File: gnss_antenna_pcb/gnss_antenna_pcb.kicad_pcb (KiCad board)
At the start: 2 copper layers, 100 x 100 mm, 38 parts, among them J1 uFL, J2 Conn_Coaxial_Power, Q1 BFP640FESD, U1 NCV8163ASN330T1G

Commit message: Update PCB
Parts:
- moved REF** 47.4 mm to (133.7, 84.8)
- moved JP2 45.2 mm to (70.0, 75.0), turned to 180 degrees
- moved R10 37.2 mm to (65.3, 81.0), turned to -90 degrees
- moved R9 36.4 mm to (64.0, 81.1), turned to 90 degrees
- moved C7 35.3 mm to (62.1, 81.4), turned to -90 degrees
- moved J1 34.9 mm to (75.0, 82.4), turned to 90 degrees
- moved U1 31.4 mm to (58.6, 81.5), turned to 0 degrees
- moved C4 28.9 mm to (62.1, 87.3), turned to 0 degrees
- moved TP1 28.4 mm to (75.0, 85.6), turned to 180 degrees
- moved C6 27.7 mm to (55.0, 81.4), turned to -90 degrees
- moved C3 25.7 mm to (65.8, 87.3), turned to 0 degrees
- moved C1 25.0 mm to (74.9, 87.5)
- moved R1 25.0 mm to (74.7, 112.0)
- moved R2 25.0 mm to (74.7, 113.0)
- moved R5 23.6 mm to (62.0, 90.3), turned to 180 degrees
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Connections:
- MW1 pad 3: Net-(C1-Pad1) -> Net-(MW1-Pad3)
- MW1 pad 4: Net-(MW1-Pad4) -> Net-(C1-Pad1)
- R1 pad 2: Net-(MW1-Pad4) -> Net-(MW1-Pad3)
- R2 pad 2: Net-(MW1-Pad4) -> Net-(MW1-Pad3)
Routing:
- net +3.3V: track 29.5 -> 0.00 mm
- net GND: track 21.7 -> 0.00 mm, vias 136 -> 65
- net Net-(C1-Pad2): track 7.66 -> 27.3 mm
- net +5V: track 15.7 -> 0.00 mm
- net Net-(C3-Pad1): track 9.48 -> 0.00 mm
- net Net-(C4-Pad1): track 7.78 -> 0.00 mm
- net Net-(C5-Pad2): track 15.1 -> 7.82 mm
- net Net-(C2-Pad2): track 7.22 -> 0.00 mm
- net Net-(R10-Pad2): track 3.97 -> 0.00 mm
- net Net-(L2-Pad1): track 1.69 -> 0.00 mm
- net Net-(MW1-Pad4): track 1.35 -> 0.00 mm
- net Net-(MW1-Pad3): track 0.00 -> 1.26 mm
- net Net-(C1-Pad1): track 1.26 -> 0.00 mm
- removed copper zone on B.Cu, net GND
- removed copper zone on F.Cu, net GND
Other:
- board text added: "Copyright (C) 2023 The Antenna Guy"

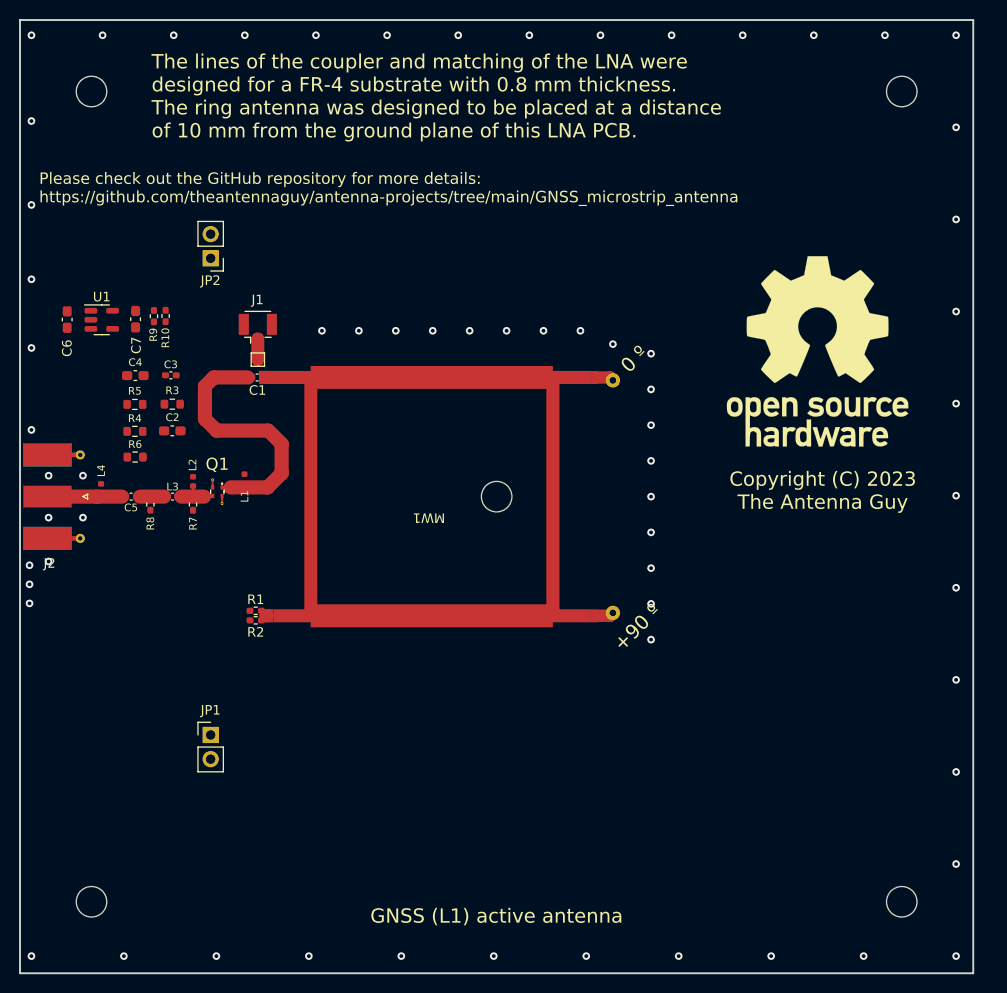
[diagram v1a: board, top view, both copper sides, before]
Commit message: Finish PCB + generate fabrication files
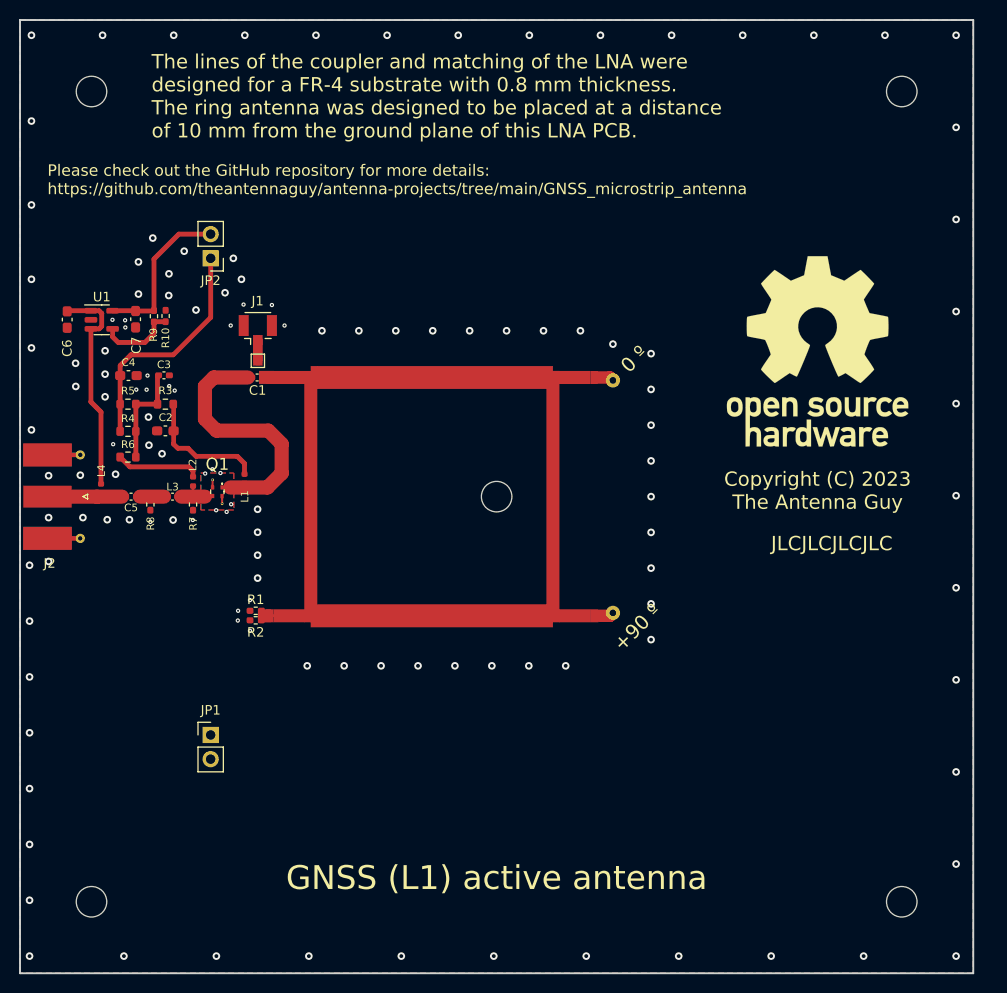
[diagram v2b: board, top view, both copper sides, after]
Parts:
- moved R6 0.75 mm to (61.3, 95.8)
- moved R5 0.73 mm to (61.3, 90.3)
- moved C3 0.73 mm to (65.1, 87.3)
- moved C4 0.73 mm to (61.4, 87.3)
- moved C2 0.72 mm to (65.2, 93.1)
- moved R3 0.72 mm to (65.2, 90.3)
- moved R4 0.72 mm to (61.3, 93.2)
- moved J1 0.12 mm to (75.0, 82.5)
- moved TP1 0.12 mm to (75.0, 85.8)
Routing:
- net Net-(C4-Pad1): track 0.00 -> 24.7 mm
- net +5V: track 0.00 -> 23.1 mm
- net +3.3V: track 0.00 -> 16.8 mm
- net Net-(C2-Pad2): track 0.00 -> 13.6 mm
- net Net-(C3-Pad1): track 0.00 -> 10.9 mm
- net Net-(L2-Pad1): track 0.00 -> 8.83 mm
- net Net-(R10-Pad2): track 0.00 -> 8.25 mm
- net GND: vias 65 -> 128
- added copper zone on B.Cu, net GND
- added copper zone on F.Cu, net GND
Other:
- board text removed: "There's an unconneted segment between the matching microstrip line. This is because the line was done witha graphic and not with a track. This was required to ensure to correct length and width of the line. You can ignore this error in the DRC since it is well connected."
